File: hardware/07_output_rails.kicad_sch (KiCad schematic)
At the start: 5 parts, among them J2 16-pin IDC POWER OUT, J7 Manual IDC wire landing

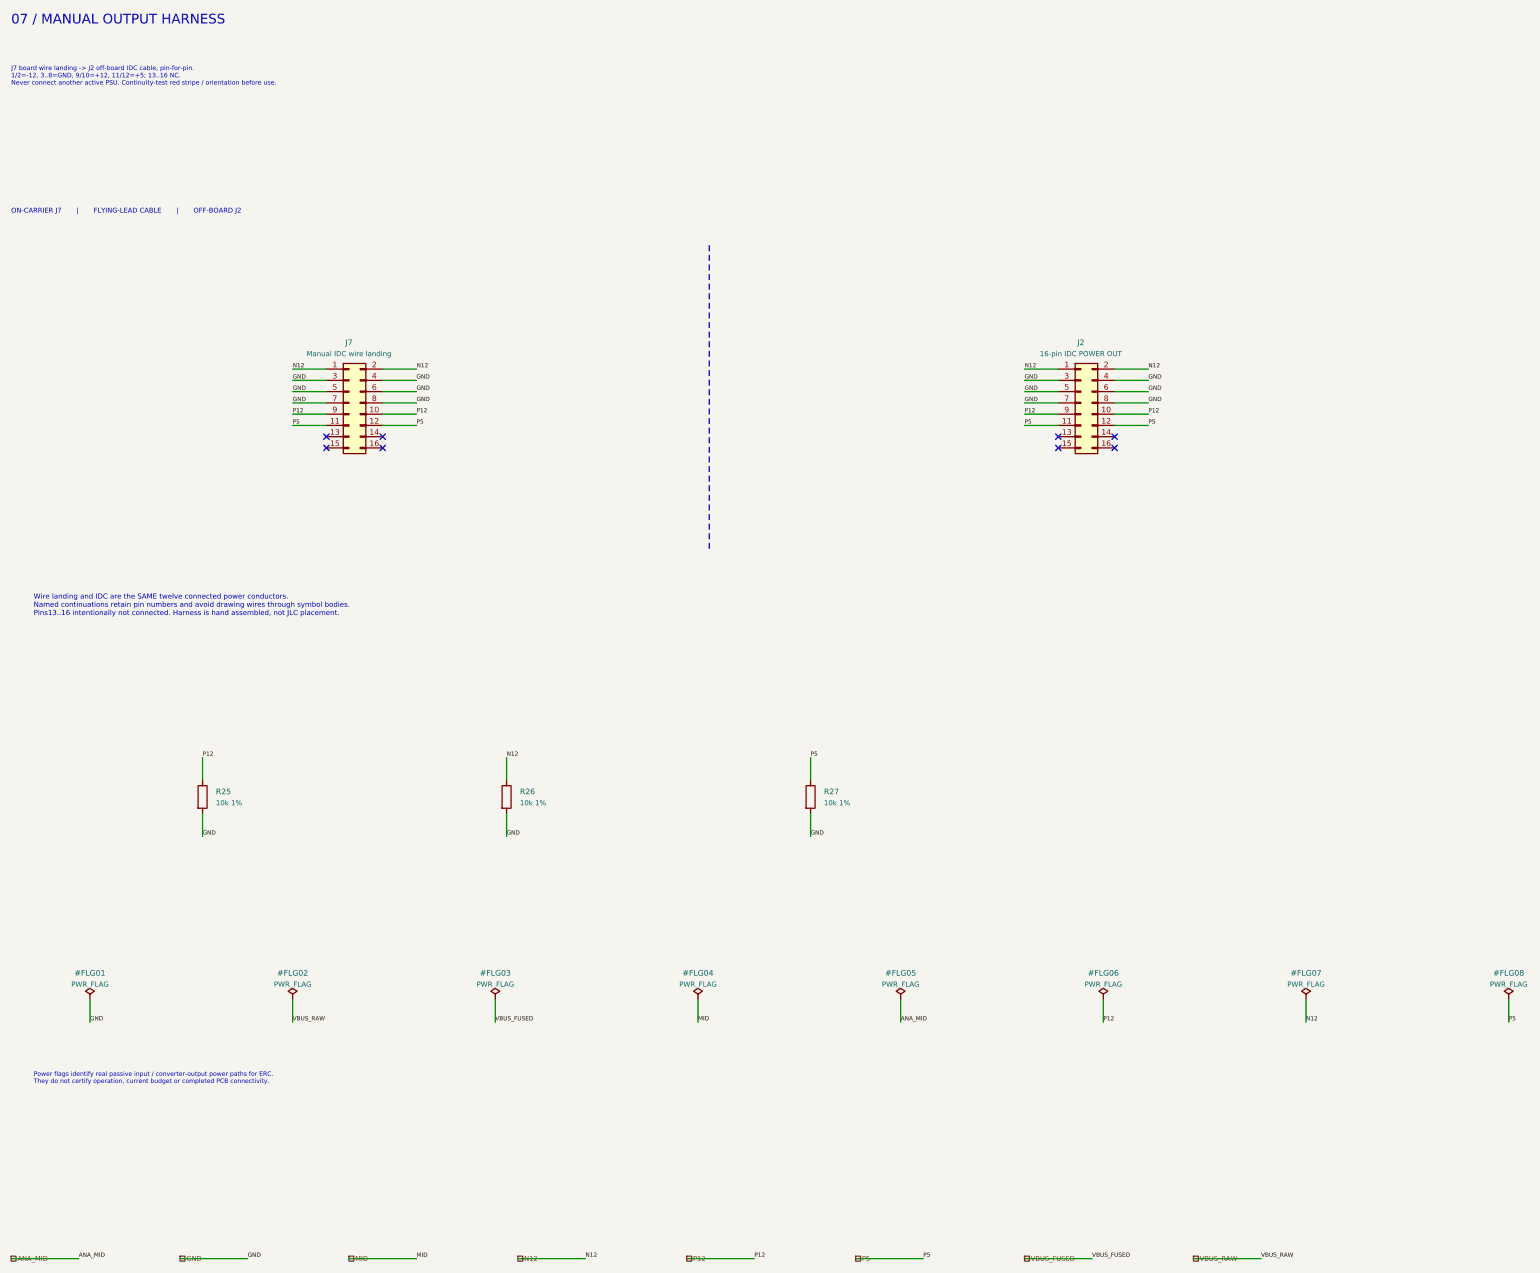
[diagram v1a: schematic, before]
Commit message: Clarify hierarchical ports and replace local label islands with visible schematic wiring
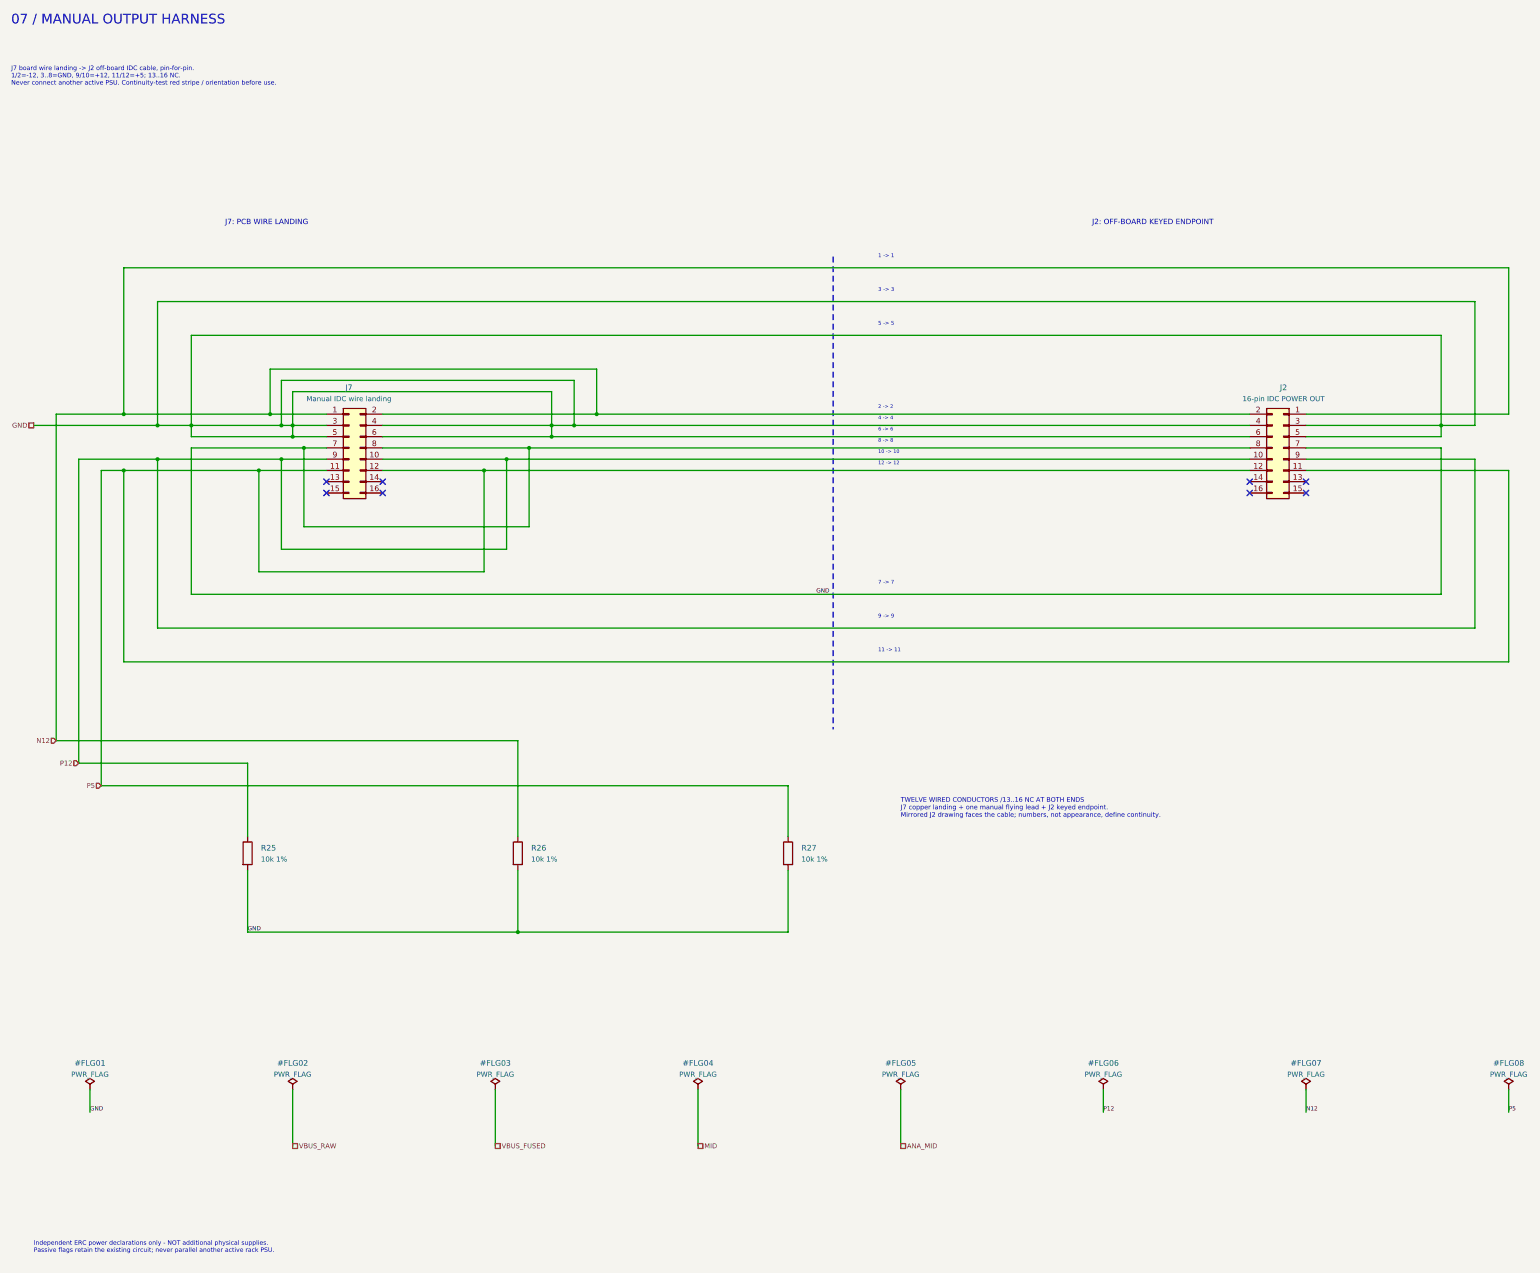
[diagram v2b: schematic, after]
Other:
- note added: "1 -> 1"
- note added: "10 -> 10"
- note added: "11 -> 11"
- note added: "12 -> 12"
- note added: "2 -> 2"
- note added: "3 -> 3"
- note added: "4 -> 4"
- note added: "5 -> 5"
- note added: "6 -> 6"
- note added: "7 -> 7"
- note added: "8 -> 8"
- note added: "9 -> 9"
- note added: "Independent ERC power declarations only - NOT additional physical supplies. Passive flags retain the existing circuit; never parallel another active rack PSU."
- note added: "J2: OFF-BOARD KEYED ENDPOINT"
- note added: "J7: PCB WIRE LANDING"
- note added: "TWELVE WIRED CONDUCTORS /13..16 NC AT BOTH ENDS J7 copper landing + one manual flying lead + J2 keyed endpoint. Mirrored J2 drawing faces the cable; numbers, not appearance, define continuity."
- note removed: "ON-CARRIER J7 | FLYING-LEAD CABLE | OFF-BOARD J2"
- note removed: "Power flags identify real passive input / converter-output power paths for ERC. They do not certify operation, current budget or completed PCB connectivity."
- note removed: "Wire landing and IDC are the SAME twelve connected power conductors. Named continuations retain pin numbers and avoid drawing wires through symbol bodies. Pins13..16 intentionally not connected. Harness is hand assembled, not JLC placement."
- moved on the sheet: J2, J7, R25, R26, R27

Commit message: Simplify V1 power architecture, remove auxiliary sensing and obsolete documentation, enable autonomous protected start and reset button
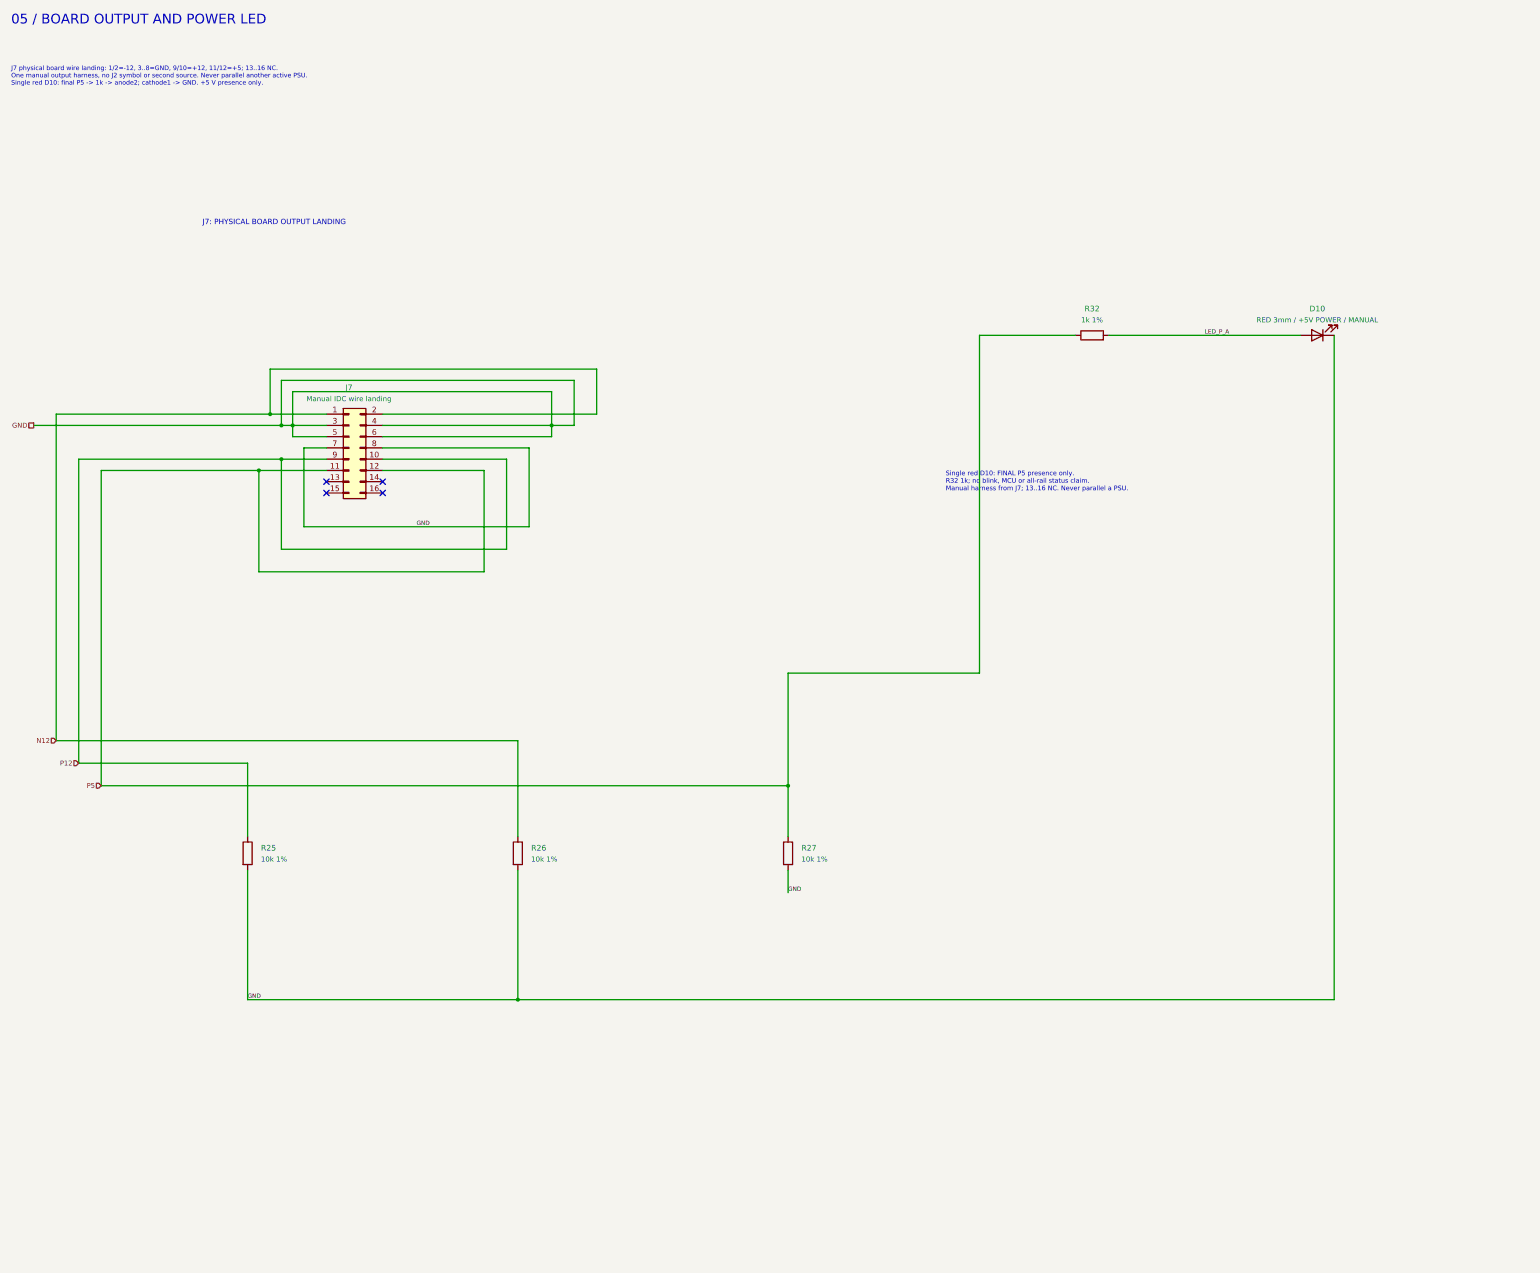
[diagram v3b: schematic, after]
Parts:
- removed J2: 16-pin IDC POWER OUT, symbol BigModular:Connector_Generic_Conn_02x08_Odd_Even
- added D10: RED 3mm / +5V POWER / MANUAL, BigModular:LED_D3.0mm_Horizontal_O1.27mm_Z2.0mm_Edge, symbol BigModular:Device_LED
- added R32: 1k 1%, BigModular:R_0603_1608Metric, symbol BigModular:Device_R
- J7: NOTE ON-CARRIER numbered solder lands, not an extra purchasable box header. Physical cable boundary to off-board J2; one power output harness, not two sources. NOT debug J8. -> ON-CARRIER numbered solder lands, not an extra purchasable box header. Physical output cable boundary; single output, never another active source.
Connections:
- net GND: now also D10.1 (K)
- net P5: now also R32.1
- new net LED_P_A: D10.2 (A), R32.2
- no-connect marks 8 -> 4
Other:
- note added: "05 / BOARD OUTPUT AND POWER LED"
- note added: "J7 physical board wire landing: 1/2=-12, 3..8=GND, 9/10=+12, 11/12=+5; 13..16 NC. One manual output harness, no J2 symbol or second source. Never parallel another active PSU. Single red D10: final P5 -> 1k -> anode2; cathode1 -> GND. +5 V presence only."
- note added: "J7: PHYSICAL BOARD OUTPUT LANDING"
- note added: "Single red D10: FINAL P5 presence only. R32 1k; no blink, MCU or all-rail status claim. Manual harness from J7; 13..16 NC. Never parallel a PSU."
- note removed: "07 / MANUAL OUTPUT HARNESS"
- note removed: "1 -> 1"
- note removed: "10 -> 10"
- note removed: "11 -> 11"
- note removed: "12 -> 12"
- note removed: "2 -> 2"
- note removed: "3 -> 3"
- note removed: "4 -> 4"
- note removed: "5 -> 5"
- note removed: "6 -> 6"
- note removed: "7 -> 7"
- note removed: "8 -> 8"
- note removed: "9 -> 9"
- note removed: "Independent ERC power declarations only - NOT additional physical supplies. Passive flags retain the existing circuit; never parallel another active rack PSU."
- note removed: "J2: OFF-BOARD KEYED ENDPOINT"
- note removed: "J7 board wire landing -> J2 off-board IDC cable, pin-for-pin. 1/2=-12, 3..8=GND, 9/10=+12, 11/12=+5; 13..16 NC. Never connect another active PSU. Continuity-test red stripe / orientation before use."
- note removed: "J7: PCB WIRE LANDING"
- note removed: "TWELVE WIRED CONDUCTORS /13..16 NC AT BOTH ENDS J7 copper landing + one manual flying lead + J2 keyed endpoint. Mirrored J2 drawing faces the cable; numbers, not appearance, define continuity."
- title: Big Modular - Manual output harness -> Big Modular - Board output and power LED

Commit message: Move USB, retry button and power LED to top; synchronize 64 V1 footprints without routing
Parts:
- D10: NOTE Single hand-soldered red3mm power LED: P5 -> R32 1k -> anode2; cathode1 GND. No automatic blink, no external control, not proof all rails are healthy. Retains original D10 hole/formed-lead fit; exact MPN pending. -> Single hand-soldered red3mm power LED: P5 -> R32 1k -> anode2; cathode1 GND. No automatic blink, no external control, not proof all rails are healthy. Top-cluster D10 hole/formed-lead envelope; exact MPN pending.

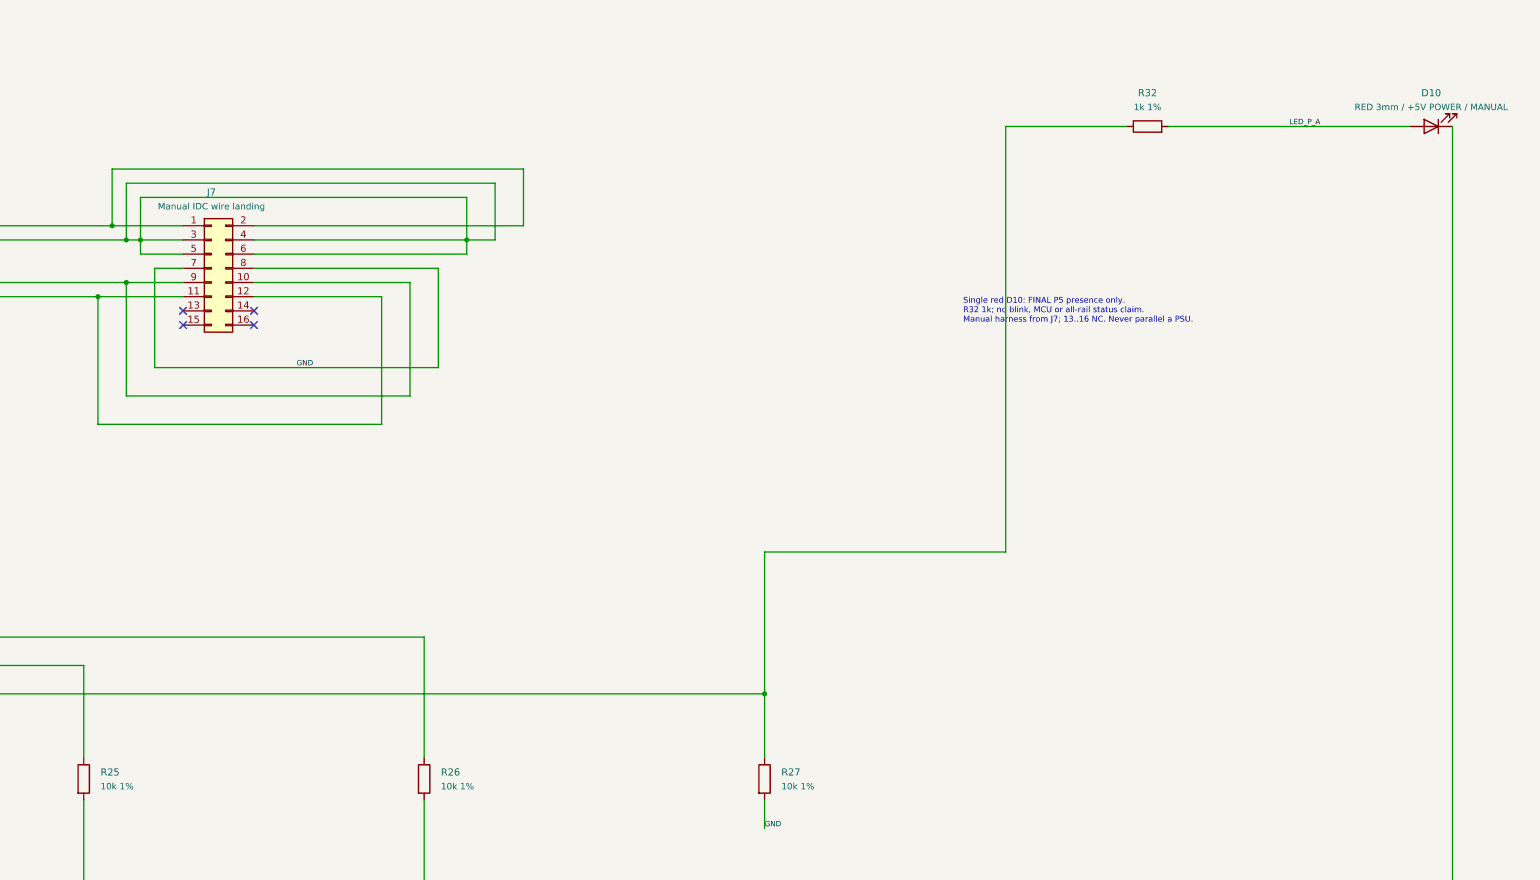
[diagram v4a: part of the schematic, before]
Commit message: Complete four-layer routing, adopt proven HRO USB-C and release checked fabrication files
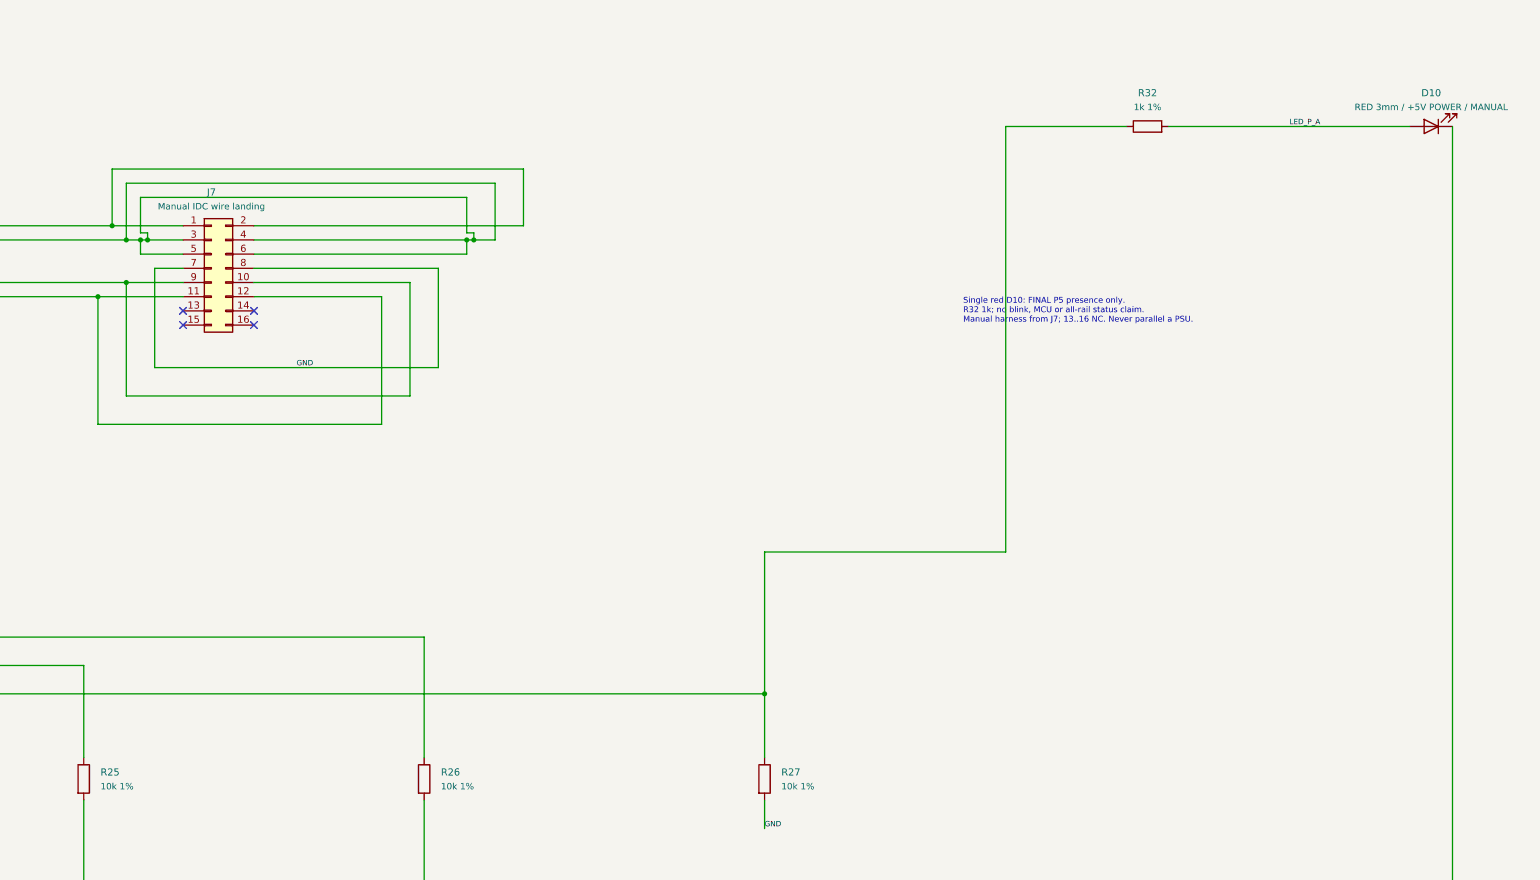
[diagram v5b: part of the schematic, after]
